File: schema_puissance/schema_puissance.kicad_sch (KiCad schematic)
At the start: 53 parts, among them J1 Conn_01x02, Q1 PN2222A, Q2 PN2222A, Q3 PN2222A, Q4 PN2222A, Q5 PN2222A, Q6 PN2222A, Q7 PN2222A, Q8 PN2222A, U1 FOD814A, U10 RT114, U11 FOD814A, U12 RT114, U13 FOD814A, U14 RT114, U15 FOD814A, U16 RT114, U2 RT114, U3 FOD814A, U4 RT114, U5 FOD814A, U6 RT114, U7 FOD814A, U8 RT114, U9 FOD814A

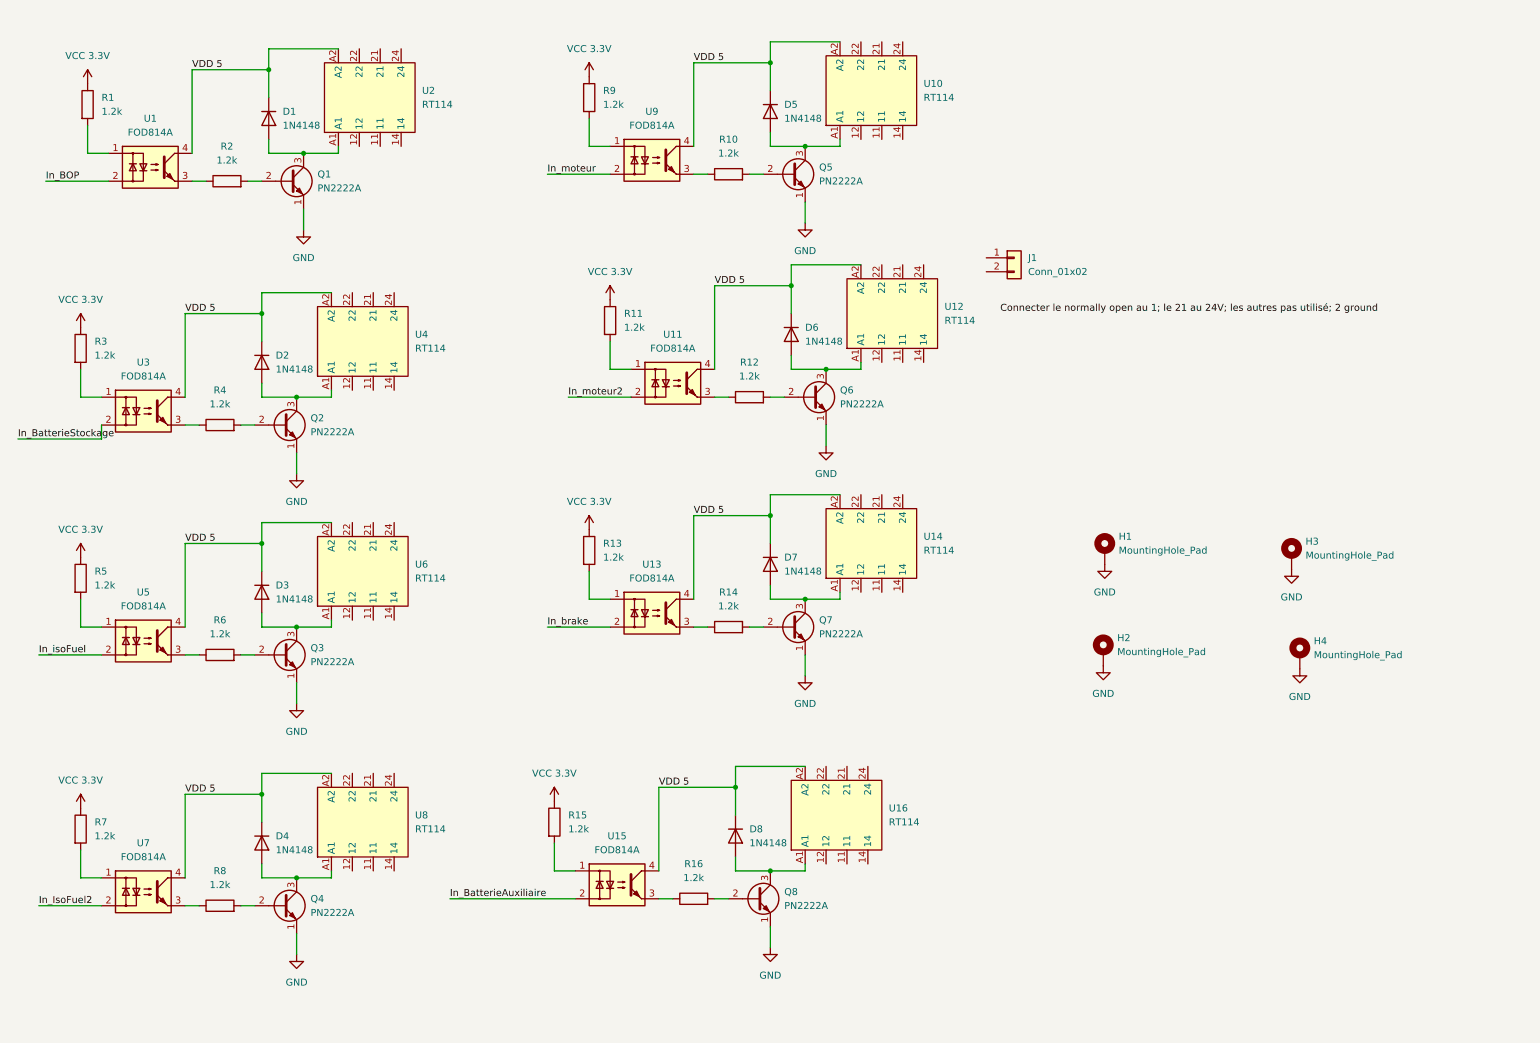
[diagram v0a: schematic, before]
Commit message: Modification 3 : connecteurs mis, routes tracées, layers faits. Il manque le connecteur pour les input et comment les relier au input
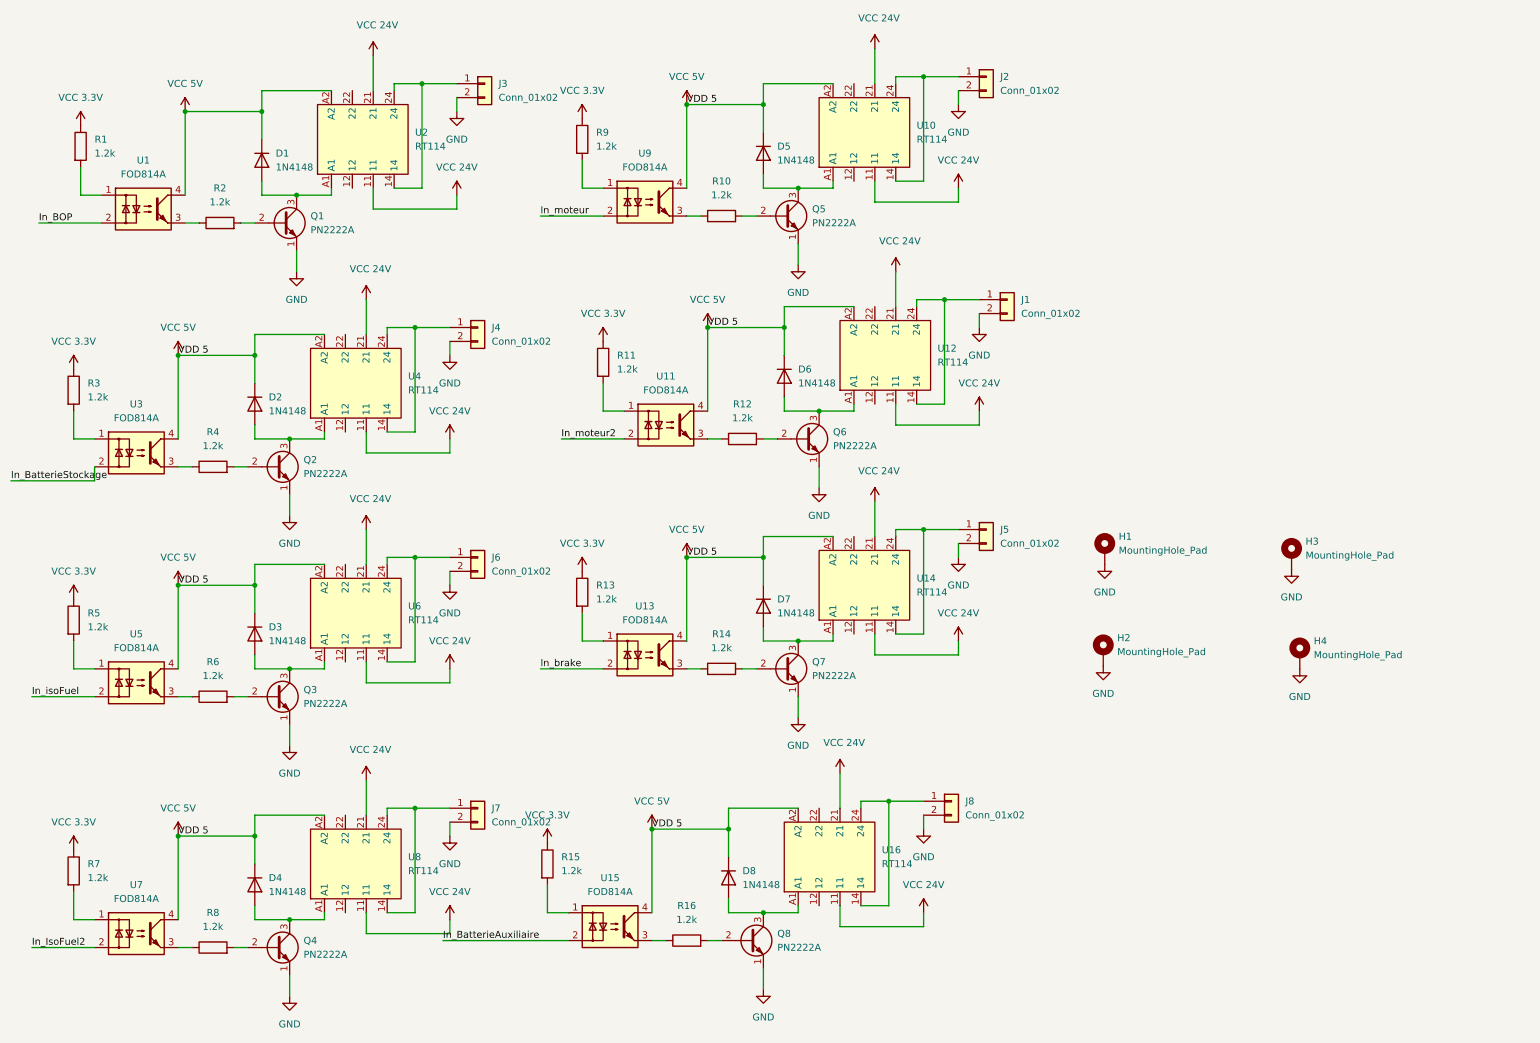
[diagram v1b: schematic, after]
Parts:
- added J2, J3, J4, J5, J6, J7, J8: Conn_01x02, TerminalBlock:TerminalBlock_MaiXu_MX126-5.0-02P_1x02_P5.00mm, symbol Connector_Generic:Conn_01x02
- J1: footprint (none) -> TerminalBlock:TerminalBlock_MaiXu_MX126-5.0-02P_1x02_P5.00mm
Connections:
- net GND: now also J1.2 (Pin_2), J2.2 (Pin_2), J3.2 (Pin_2), J4.2 (Pin_2), J5.2 (Pin_2), J6.2 (Pin_2), J7.2 (Pin_2), J8.2 (Pin_2)
- net VCC 24V: now reaches U4.11
- net VCC 24V: now also U10.11, U10.21, U12.11, U12.21, U14.11, U14.21, U16.11, U16.21, U2.11, U2.21, U4.21, U6.11, U6.21, U8.11, U8.21
- net at U4.14: now also U4.24, J4.1 (Pin_1)
- net at U10.14: now also U10.24, J2.1 (Pin_1)
- net at U2.14: now also U2.24, J3.1 (Pin_1)
- net at J1.1 (Pin_1): now also U12.14, U12.24
- net at U14.14: now also U14.24, J5.1 (Pin_1)
- net at U8.14: now also U8.24, J7.1 (Pin_1)
- net at U6.14: now also U6.24, J6.1 (Pin_1)
- net at U16.14: now also U16.24, J8.1 (Pin_1)
- net VDD 5 renamed VCC 5V
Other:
- moved on the sheet: D1, D2, D3, D4, D5, D6, D7, D8, Q1, Q2, Q3, Q4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

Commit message: version 3
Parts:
- added D10, D11, D12, D13, D14, D15, D16, D9: 1N4148, Diode_THT:D_DO-35_SOD27_P7.62mm_Horizontal, symbol Diode:1N4148
- added J9: Conn_01x25, symbol Connector_Generic:Conn_01x25
- Q1, Q2, Q3, Q4, Q5, Q6, Q7, Q8: value PN2222A -> PN2222ATA
- U10, U12, U14, U16, U2, U4, U6, U8: value RT114 -> RTD14005; symbol libra:RTT114 -> Relay:RT314A05
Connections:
- net GND: now also D10.1 (K), D11.1 (K), D12.1 (K), D13.1 (K), D14.1 (K), D15.1 (K), D16.1 (K), D9.1 (K), J9.10 (Pin_10), J9.13 (Pin_13), J9.16 (Pin_16), J9.19 (Pin_19), J9.2 (Pin_2), J9.21 (Pin_21), J9.24 (Pin_24), J9.5 (Pin_5)
- net In_BOP: now also J9.14 (Pin_14)
- net In_BatterieAuxiliaire: now also J9.12 (Pin_12)
- net In_BatterieStockage: now also J9.3 (Pin_3)
- net In_IsoFuel2: now also J9.6 (Pin_6)
- net In_brake: now also J9.23 (Pin_23)
- net In_isoFuel: now also J9.17 (Pin_17)
- net In_moteur: now also J9.20 (Pin_20)
- net In_moteur2: now also J9.9 (Pin_9)
- net VCC 24V: no longer U10.21, U12.11, U12.21, U14.21, U16.21, U2.21, U4.21, U6.21, U8.21
- net VCC 5V: now also U10.A1, U12.A1, U14.A1, U16.A1, U2.A1, U4.A1, U6.A1, U8.A1; no longer U10.A2, U12.A2, U14.A2, U16.A2, U2.A2, U4.A2, U6.A2, U8.A2
- net at D2.2 (A), Q2.3 (C): now also U14.A2; no longer U4.A1
- net at D5.2 (A), Q5.3 (C): now also U4.A2; no longer U10.A1
- net at J3.1 (Pin_1), U2.14: now also D9.2 (A); no longer U2.24
- net at D1.2 (A), Q1.3 (C): now also U2.A2; no longer U2.A1
- net at D8.2 (A), Q8.3 (C): now also U10.A2; no longer U16.A1
- net at D7.2 (A), Q7.3 (C): now also U8.A2; no longer U14.A1
- net at D6.2 (A), Q6.3 (C): now also U6.A2; no longer U12.A1
- net at D4.2 (A), Q4.3 (C): now also U12.A2; no longer U8.A1
- net at D3.2 (A), Q3.3 (C): now also U16.A2; no longer U6.A1
- new net: D10.2 (A), J2.1 (Pin_1), U4.14
- new net: D16.2 (A), J8.1 (Pin_1), U10.14
- new net: D12.2 (A), J1.1 (Pin_1), U6.14
- new net: D13.2 (A), J5.1 (Pin_1), U8.14
- new net: D15.2 (A), J7.1 (Pin_1), U12.14
- new net: D14.2 (A), J6.1 (Pin_1), U16.14
- new net: D11.2 (A), J4.1 (Pin_1), U14.14
- new net +24V: J9.1 (Pin_1), J9.15 (Pin_15), J9.18 (Pin_18), J9.4 (Pin_4), J9.7 (Pin_7)
- new net +3.3V: J9.22 (Pin_22), J9.8 (Pin_8)
- new net +5V: J9.11 (Pin_11), J9.25 (Pin_25)
- new net 24V: U12.11
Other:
- moved on the sheet: U10, U14, U16, U2, U6
